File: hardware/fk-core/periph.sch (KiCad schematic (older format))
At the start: 9 parts, among them M1 MICROSD, P5 CONN_01X04, U5 PCF8523T, U8 FGPMMOPA6H

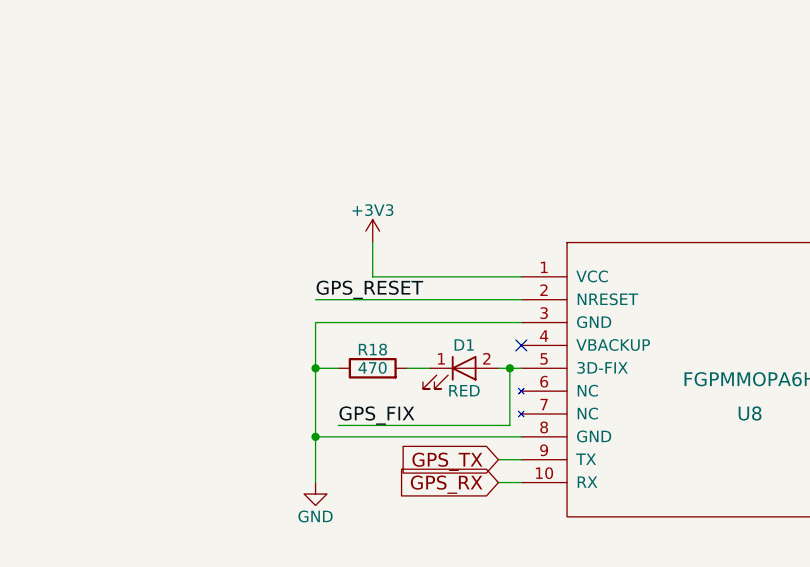
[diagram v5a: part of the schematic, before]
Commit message: Tweaking positions.
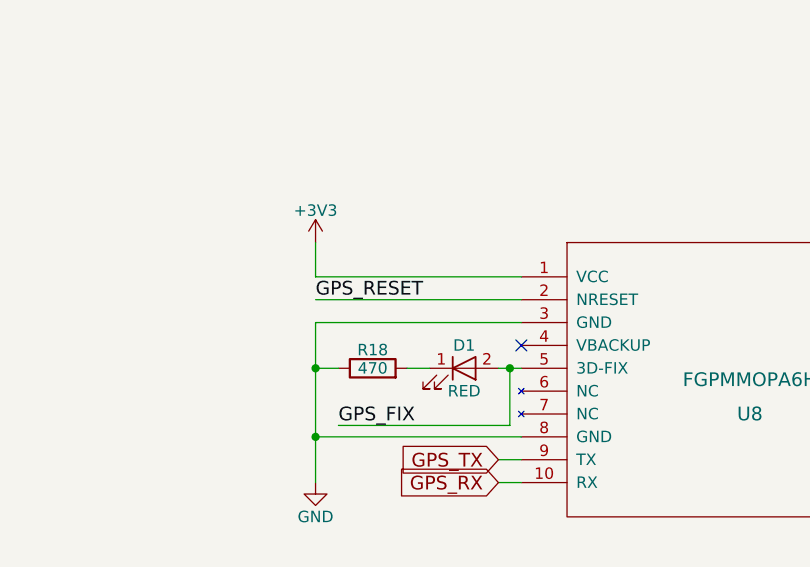
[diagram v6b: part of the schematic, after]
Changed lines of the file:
@@
 L +3V3 #PWR063
 U 1 1 58809394
-P 5350 3900
-F 0 "#PWR063" H 5350 3750 50  0001 C CNN
-F 1 "+3V3" H 5350 4040 50  0000 C CNN
-F 2 "" H 5350 3900 50  0000 C CNN
-F 3 "" H 5350 3900 50  0000 C CNN
-	1    5350 3900
+P 5100 3900
+F 0 "#PWR063" H 5100 3750 50  0001 C CNN
+F 1 "+3V3" H 5100 4040 50  0000 C CNN
+F 2 "" H 5100 3900 50  0000 C CNN
+F 3 "" H 5100 3900 50  0000 C CNN
+	1    5100 3900
 	1    0    0    -1
 $EndComp
 Wire Wire Line
-	6000 4050 5350 4050
+	6000 4050 5100 4050
 Wire Wire Line
-	5350 4050 5350 3900
+	5100 4050 5100 3900
 Text GLabel 5900 4850 0    60   Input ~ 0
 GPS_TX
@@
 $EndComp
 Wire Wire Line
-	6000 4450 5900 4450
+	5900 4450 6000 4450
 Wire Wire Line
 	5600 4450 5500 4450

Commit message: Cleaning up footprints and libraries.
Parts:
- M1: footprint microsd:MicroSD-Yamaichi-PJS -> microsd:MICROSD
- U5: footprint IPC7351-Nominal:SOIC127P600X175-8 -> SMD_Packages:SOIC-8-N
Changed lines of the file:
@@
 LIBS:microsd
 LIBS:pcf8523t
-LIBS:xtal32x15
 LIBS:tps63060
 LIBS:max1704xx
@@
 LIBS:fgpmmopa6h
 LIBS:sk6812
+LIBS:dcbarrelsmt
+LIBS:xtal-3.2x1
 LIBS:fk-core-cache
 EELAYER 25 0
@@
 F 0 "M1" H 3300 2200 45  0001 C CNN
 F 1 "MICROSD" H 3300 2200 45  0001 C CNN
-F 2 "microsd:MicroSD-Yamaichi-PJS" H 3330 2350 20  0001 C CNN
+F 2 "microsd:MICROSD" H 3330 2350 20  0001 C CNN
 F 3 "" H 3300 2200 60  0001 C CNN
 F 4 "101-00581-59-1-ND" H 3300 2200 60  0001 C CNN "SPN"
@@
 F 0 "U5" H 6700 2050 50  0000 C CNN
 F 1 "PCF8523T" H 6700 1950 50  0000 C CNN
-F 2 "IPC7351-Nominal:SOIC127P600X175-8" H 6700 850 50  0001 C CNN
+F 2 "SMD_Packages:SOIC-8-N" H 6700 850 50  0001 C CNN
 F 3 "http://www.nxp.com/documents/data_sheet/PCF8523.pdf" H 6700 750 50  0001 C CNN
 F 4 "568-5306-1-ND" H 6700 1750 60  0001 C CNN "SPN"

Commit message: Adding SMA footprint for GPS and fix XTAL.
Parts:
- AE1: footprint (none) -> SMA:SMA
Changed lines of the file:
@@
 F 0 "AE1" H 8150 5250 50  0000 C CNN
 F 1 "Antenna_Dipole" H 8150 5200 50  0000 C CNN
-F 2 "" H 8100 5200 50  0001 C CNN
+F 2 "SMA:SMA" H 8100 5200 50  0001 C CNN
 F 3 "" H 8100 5200 50  0001 C CNN
 F 4 "H11891CT-ND" H 8100 5200 60  0001 C CNN "SPN"
